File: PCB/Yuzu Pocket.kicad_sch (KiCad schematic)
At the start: 32 parts, among them J1 USB_A, U1 V3LP, U2 ULN2003, U3 ULN2003

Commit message: Schematic done!
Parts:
- added C1, C2: 18pF, Capacitor_SMD:C_0603_1608Metric_Pad1.08x0.95mm_HandSolder, symbol Device:C
- added C10, C12, C3, C8: 22uF, Capacitor_SMD:C_0603_1608Metric_Pad1.08x0.95mm_HandSolder, symbol Device:C
- added C11, C18, C19, C20, C21, C22, C23, C24, C25, C26, C27, C28, C29, C30, C31, C32, C33, C34, C35, C36, C37, C38, C39, C4, C40, C41, C5, C7: .1uF, Capacitor_SMD:C_0603_1608Metric_Pad1.08x0.95mm_HandSolder, symbol Device:C
- added C13, C14, C15, C16, C17, C6: 1uF, Capacitor_SMD:C_0603_1608Metric_Pad1.08x0.95mm_HandSolder, symbol Device:C
- added C9: 20pF, Capacitor_SMD:C_0603_1608Metric_Pad1.08x0.95mm_HandSolder, symbol Device:C
- added Card1: TF PUSH, easyeda2kicad:TF-SMD_TF-PUSH, symbol easyeda2kicad:TFPUSH
- added L1: APH252012C1R5MP01, easyeda2kicad:IND-SMD_APH252012C3R3MP01, symbol easyeda2kicad:APH252012C1R5MP01
- added R1, R10, R14, R2, R8: 10k, Resistor_SMD:R_0603_1608Metric_Pad0.98x0.95mm_HandSolder, symbol Device:R
- added R12: 39k, Resistor_SMD:R_0603_1608Metric_Pad0.98x0.95mm_HandSolder, symbol Device:R
- added R13: 78k, Resistor_SMD:R_0603_1608Metric_Pad0.98x0.95mm_HandSolder, symbol Device:R
- added R19, R21, R23, R25, R27: 47k, Resistor_SMD:R_0603_1608Metric_Pad0.98x0.95mm_HandSolder, symbol Device:R
- added R3: 0, Resistor_SMD:R_0603_1608Metric_Pad0.98x0.95mm_HandSolder, symbol Device:R
- added SW1, SW2: LXW-52X52X2-SMD, easyeda2kicad:SW-SMD_4P-L5.2-W5.2-P5.80-LS6.4, symbol easyeda2kicad:LXW-52X52X2-SMD
- added TP1, TP2, TP3, TP4, TP5, TP6: TestPoint, TestPoint:TestPoint_Pad_D1.5mm, symbol Connector:TestPoint
- added TP7: UART0_RX, TestPoint:TestPoint_Pad_D1.5mm, symbol Connector:TestPoint
- added TP8: UART0_TX, TestPoint:TestPoint_Pad_D1.5mm, symbol Connector:TestPoint
- added U1: 3225 24M 12PF 10PPM, easyeda2kicad:CRYSTAL-SMD_4P-L3.2-W2.5-BL, symbol easyeda2kicad:322524M12PF10PPM
- added U3: USBLC6-2SC6, Package_TO_SOT_SMD:SOT-23-6, symbol Power_Protection:USBLC6-2SC6
- added U4: W25Q256JVFIQT, easyeda2kicad:SOIC-16_L10.3-W7.5-P1.27-LS10.3-BL, symbol easyeda2kicad:W25Q256JVFIQT
- added U5: TMI3253S, easyeda2kicad:SOT-23-6_L2.9-W1.6-P0.95-LS2.8-BL, symbol easyeda2kicad:TMI3253S
- added U8: ME6211C15M5, Package_TO_SOT_SMD:SOT-23-5, symbol Regulator_Linear:ME6211C15M5
- added U9: ME6211C33M5, Package_TO_SOT_SMD:SOT-23-5, symbol Regulator_Linear:ME6211C33M5
- U2: footprint (none) -> Package_SO:SOIC-16_3.9x9.9mm_P1.27mm
- U6: renamed from U3; footprint (none) -> Package_SO:SOIC-16_3.9x9.9mm_P1.27mm
- renumbered R6 to R11, R7 to R15, R8 to R16, R9 to R17, R10 to R18, R11 to R20, R12 to R22, R13 to R24, R14 to R26, R1 to R4, R2 to R5, R3 to R6, R4 to R7, R5 to R9, U1 to U10
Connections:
- net +1.2V: now also C10.2, C12.2, C18.2, C20.2, C22.2, C24.2, C26.2, C28.2, C30.2, C32.2, C34.2, C36.2, C9.2, L1.2, R12.1, TP3.1
- net +1.5V: now also C15.1, C38.2, C39.2, C40.2, C41.2, TP4.1, U8.5 (V_{OUT})
- net +3.3V: now also C11.2, C13.2, C17.1, C19.2, C21.2, C23.2, C25.2, C27.2, C29.2, C31.2, C33.2, C35.2, C37.2, C4.2, C6.2, Card1.4 (VDD), R1.1, R10.1, R14.1, R19.1, R2.1, R21.1, R23.1, R25.1, R27.1, R8.1, TP5.1, U4.2 (VCC), U9.5 (V_{OUT})
- net +5V: now also C14.2, C16.2, C3.2, C7.2, C8.2, U3.5 (VBUS), U5.4 (EN), U5.5 (IN), U8.1 (V_{IN}), U8.3 (CE), U9.1 (V_{IN}), U9.3 (CE)
- net GND: now also C1.2, C10.1, C11.1, C12.1, C13.1, C14.1, C15.2, C16.1, C17.2, C18.1, C19.1, C2.2, C20.1, C21.1, C22.1, C23.1, C24.1, C25.1, C26.1, C27.1, C28.1, C29.1, C3.1, C30.1, C31.1, C32.1, C33.1, C34.1, C35.1, C36.1, C37.1, C38.1, C39.1, C4.1, C40.1, C41.1, C6.1, C7.1, C8.1, Card1.10, Card1.11, Card1.12, Card1.13, Card1.6 (VSS), R13.2, SW1.3, SW1.4, SW2.3, SW2.4, TP6.1, U1.2 (GND), U1.4 (GND), U3.2 (GND), U4.10 (GND), U5.2 (GND), U8.2 (V_{SS}), U9.2 (V_{SS})
- net LEDG1: now also U10.30 (PE7)
- net LEDG2: now also U10.28 (PE8)
- net LEDG3: now also U10.27 (PE9)
- net LEDG4: now also U10.24 (PE10)
- net LEDG5: now also U10.23 (PE11)
- net LEDG6: now also U10.22 (PE12)
- net LEDG7: now also U10.18 (PE13)
- net LEDR1: now also U10.37 (PE0)
- net LEDR2: now also U10.36 (PE1)
- net LEDR3: now also U10.35 (PE2)
- net LEDR4: now also U10.34 (PE3)
- net LEDR5: now also U10.33 (PE4)
- net LEDR6: now also U10.32 (PE5)
- net LEDR7: now also U10.31 (PE6)
- net USB D+: now also U3.6 (I/O1); no longer J1.3 (D+)
- net USB D-: now also U3.4 (I/O2); no longer J1.2 (D-)
- net DAT2: now reaches U10.101 (PF5)
- net DAT2: now also Card1.1 (DAT2), R23.2
- net DAT3: now reaches U10.102 (PF4)
- net DAT3: now also Card1.2 (CD/DAT3), R25.2
- net SD_CMD: now reaches U10.103 (PF3)
- net SD_CMD: now also Card1.3 (CMD), R27.2
- net SD_CLK: now reaches U10.105 (PF2)
- net SD_CLK: now also Card1.5 (CLX)
- net DAT0: now reaches U10.106 (PF1)
- net DAT0: now also Card1.7 (DAT0), R19.2
- net DAT1: now reaches U10.107 (PF0)
- net DAT1: now also Card1.8 (DAT1), R21.2
- net at U10.48 (PB8): now also TP8.1
- net at U10.49 (PB9): now also TP7.1
- net FLASH_DO: now reaches U10.52 (PC0)
- net FLASH_DO: now also U4.8 (DO(IO1))
- net FLASH_CLK: now reaches U10.53 (PC1)
- net FLASH_CLK: now also U4.16 (CLK)
- net FLASH_CS: now reaches U10.54 (PC2)
- net FLASH_CS: now also R3.1
- net FLASH_DI: now reaches U10.55 (PC3)
- net FLASH_DI: now also U4.15 (DI(IO0))
- net X24MOUT: now reaches U10.74 (X24MOUT)
- net X24MOUT: now also C2.1, U1.3 (OSC2)
- net X24MIN: now reaches U10.75 (X24MIN)
- net X24MIN: now also C1.1, U1.1 (OSC1)
- net RESET: now reaches U10.99 (RESET)
- net RESET: now also R1.2, SW1.1, SW1.2, TP1.1
- new net: C5.1, U5.1 (BS)
- new net: C9.1, R12.2, R13.1, U5.3 (FB)
- new net: C5.2, L1.1, U5.6 (LX)
- new net: J1.3 (D+), U3.1 (I/O1)
- new net: J1.2 (D-), U3.3 (I/O2)
- new net: R3.2, U4.7 (~{CS})
- new net BOOT: R2.2, SW2.1, SW2.2, TP2.1
- new net FLASH_RESET: R10.2, U4.3 (~{RESET})
- new net FLASH_RESET#: R8.2, U4.1 (RESET#(IO3))
- new net FLASH_WP: R14.2, U4.9 (WP#(IO2))
- no-connect marks 11 -> 19
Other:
- note added: "BUTTONS"
- note added: "CLOCK"
- note added: "POWER & USB"
- note added: "SPI FLASH & SD CARD"
- moved on the sheet: D1, D10, D11, D12, D13, D14, D2, D3, D4, D5, D6, D7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

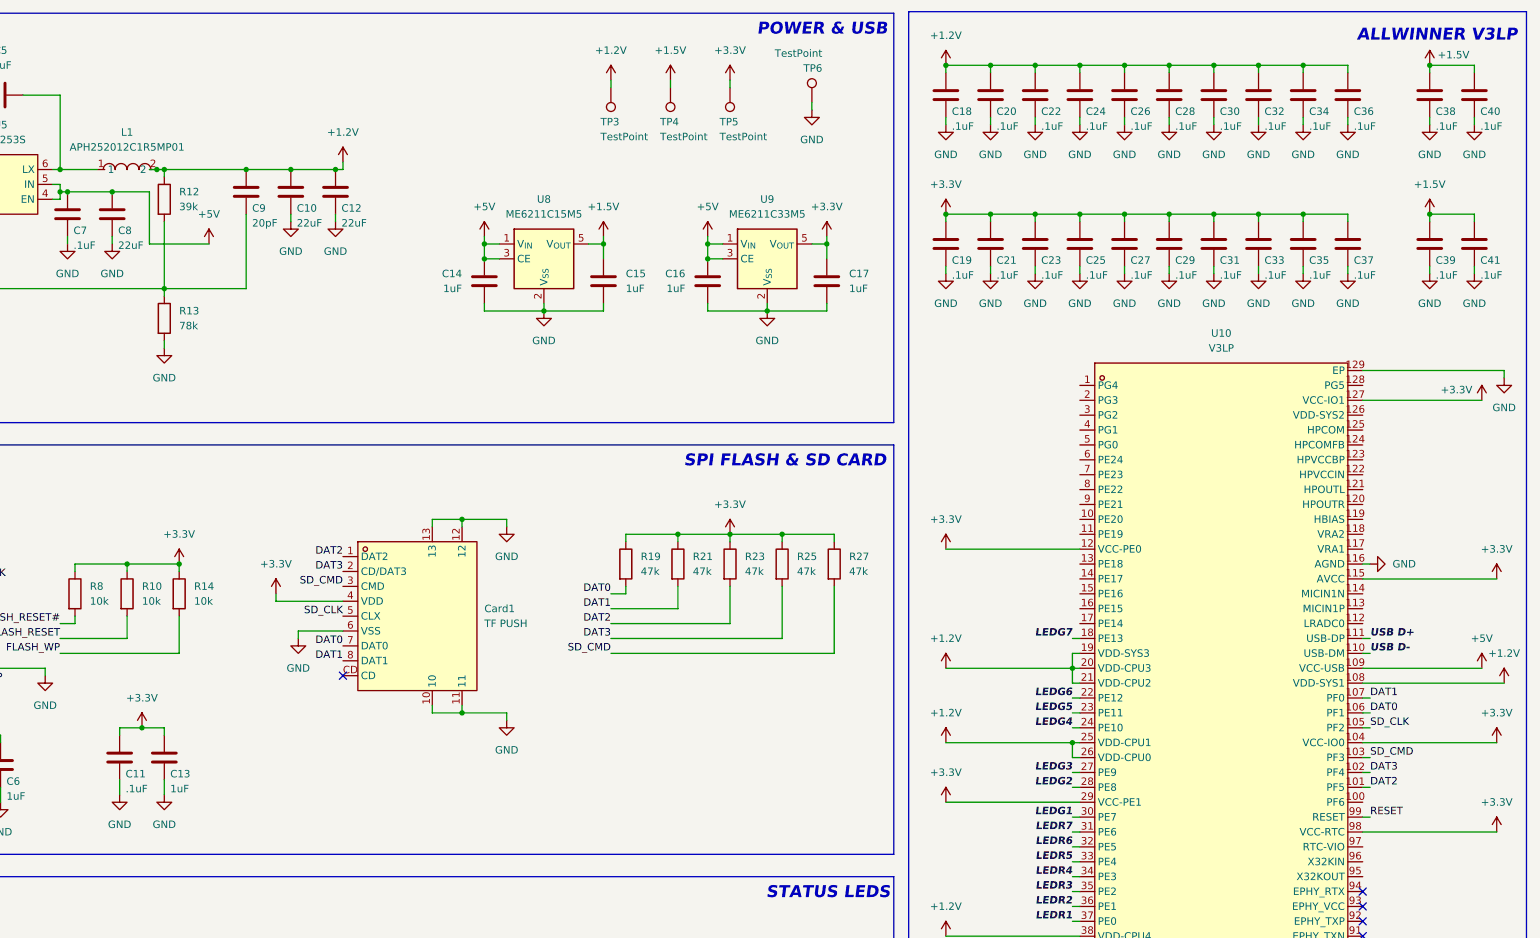
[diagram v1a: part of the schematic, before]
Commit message: PCB Layout + Routing Done
The business card is ready for silkscreen!
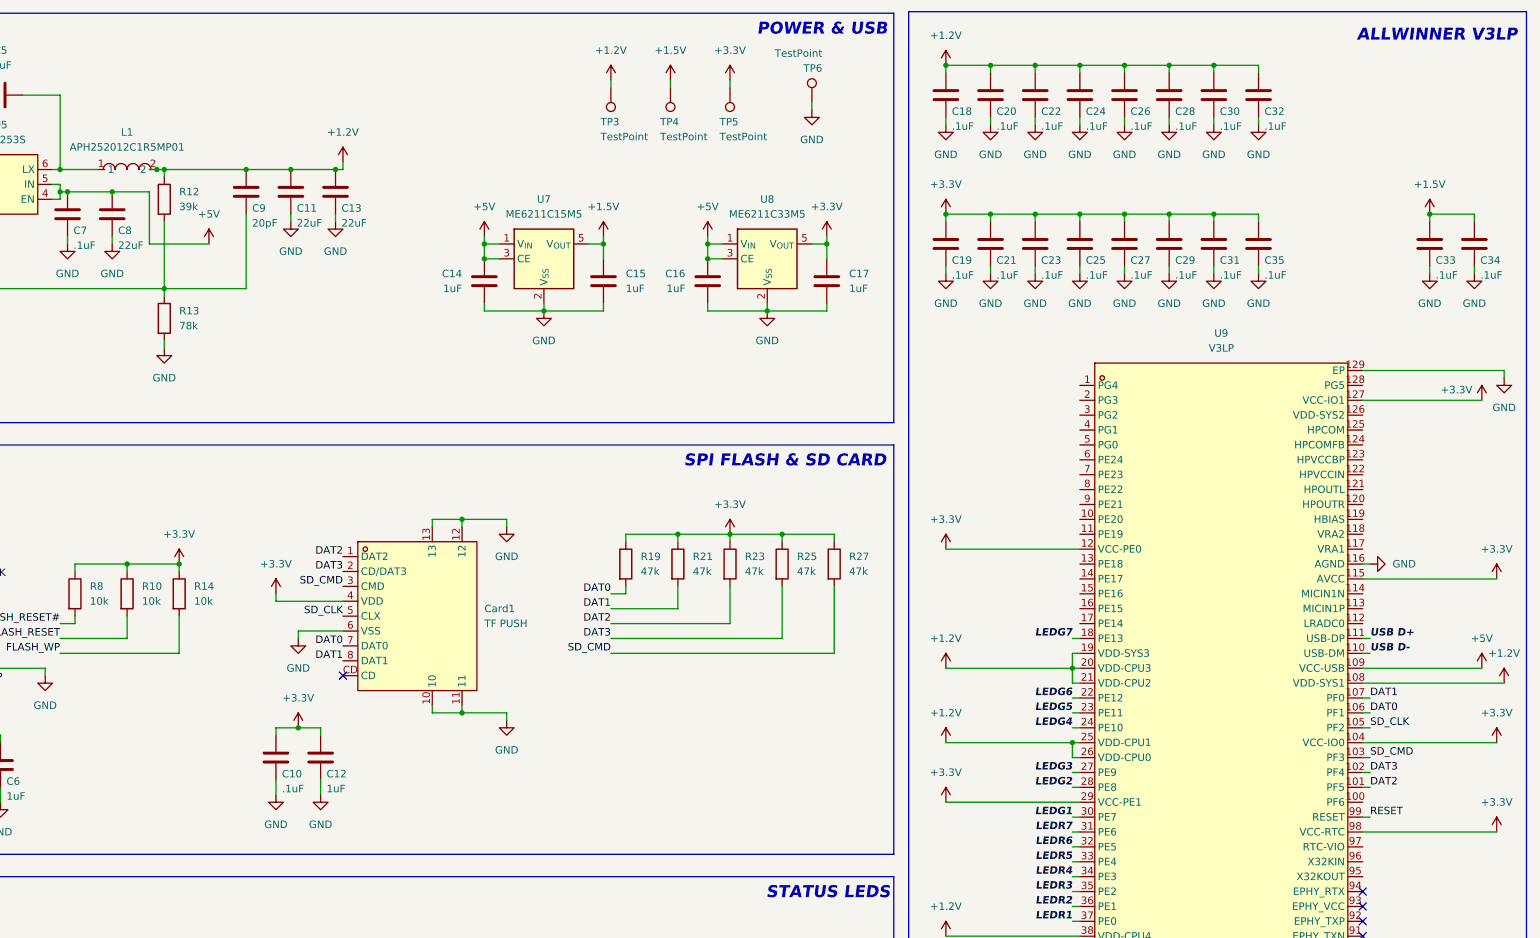
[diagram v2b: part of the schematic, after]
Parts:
- removed C33, C34, C36, C37, C38, C40: .1uF, Capacitor_SMD:C_0603_1608Metric_Pad1.08x0.95mm_HandSolder, symbol Device:C
- renumbered C11 to C10, C10 to C11, C13 to C12, C12 to C13, C39 to C33, C41 to C34, U8 to U7, U9 to U8, U10 to U9
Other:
- moved on the sheet: C10, C12
